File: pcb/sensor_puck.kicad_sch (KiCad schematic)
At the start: 67 parts, among them J1 DISP LEFT, J2 DISP RIGHT, J3 USB_C_Receptacle_USB2.0_16P, J5 Generic, SW1 RST, SW2 BOOT, U1 ESP32-S3-MINI-1U, U2 ST25DV16K-IER8C3, U3 LSM6DSOXTR, U4 STC31-C-R3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

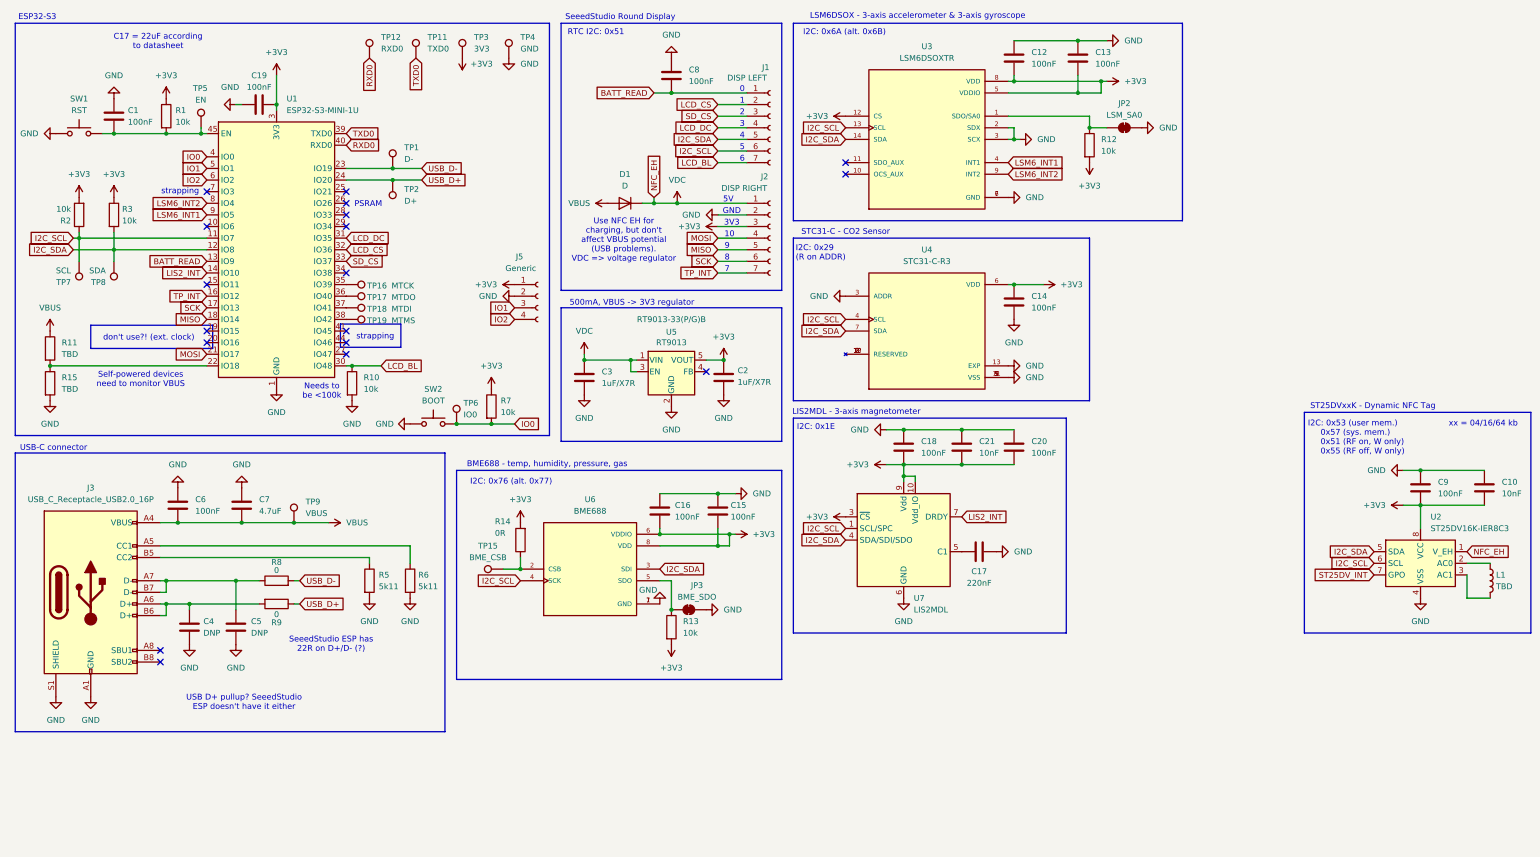
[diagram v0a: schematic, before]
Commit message: feat(schematic): add resettable fuses to VBUS and 3V3 for short protection
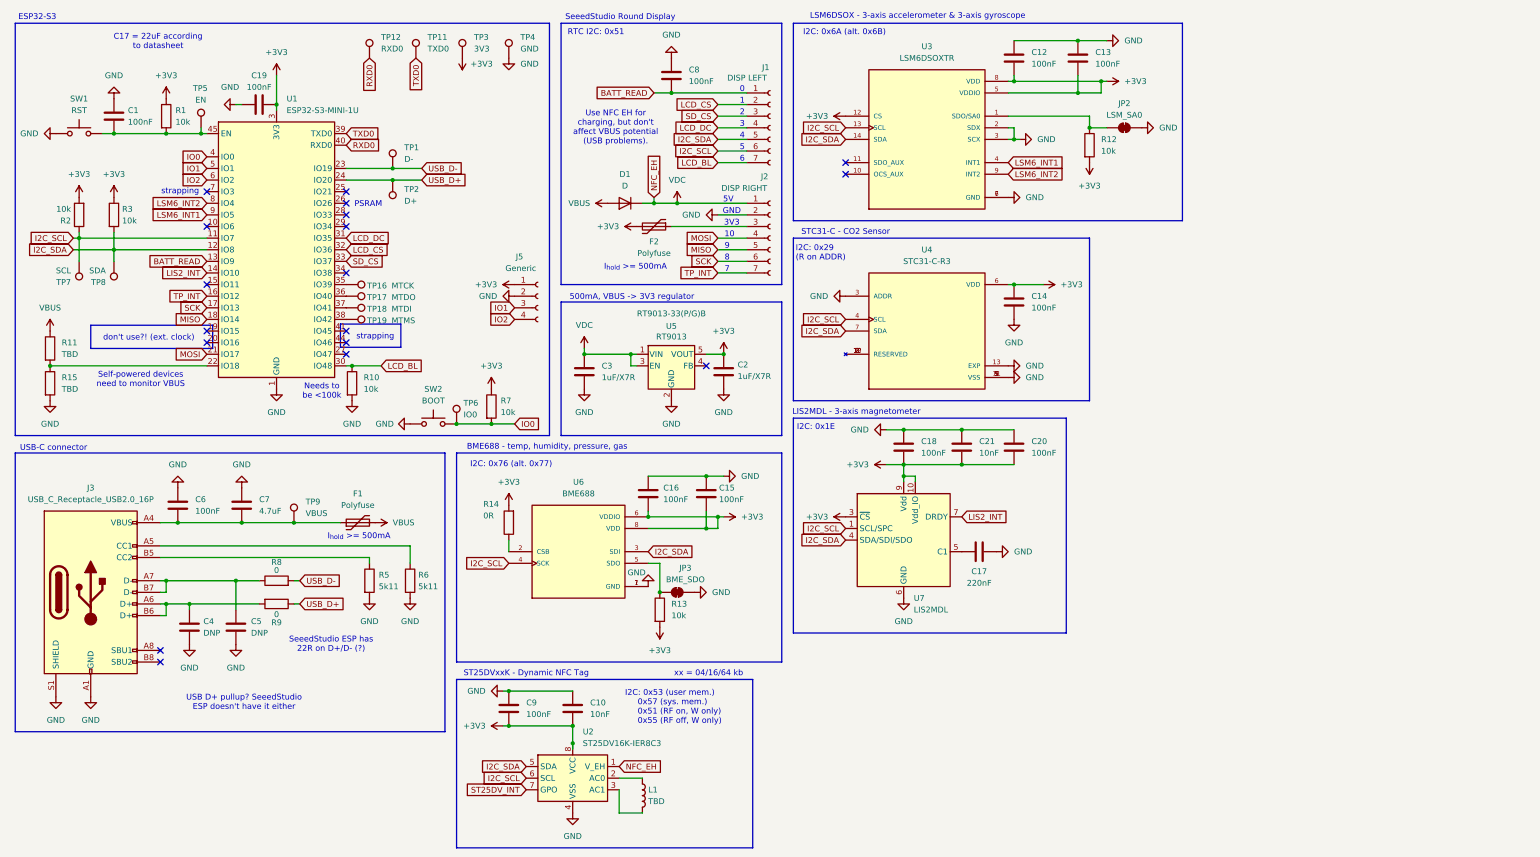
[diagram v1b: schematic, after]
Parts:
- removed TP15: BME_CSB, TestPoint:TestPoint_Pad_D1.0mm, symbol Connector:TestPoint
- added F1, F2: Polyfuse, symbol Device:Polyfuse
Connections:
- net +3V3: now also F2.2; no longer J2.3 (Pin_3)
- net VBUS: now also F1.2; no longer C6.2, C7.2, J3.A4 (VBUS), J3.A9 (VBUS), J3.B4 (VBUS), J3.B9 (VBUS), TP9.1
- new net: F2.1, J2.3 (Pin_3)
- new net: C6.2, C7.2, F1.1, J3.A4 (VBUS), J3.A9 (VBUS), J3.B4 (VBUS), J3.B9 (VBUS), TP9.1
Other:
- note added: "I_{hold} >= 500mA"
- note added: "Use NFC EH for charging, but don't affect VBUS potential (USB problems)."
- note removed: "Use NFC EH for charging, but don't affect VBUS potential (USB problems). VDC => voltage regulator"
- moved on the sheet: C10, C15, C16, C2, C3, C9, JP3, L1, R13, R14, U2, U5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

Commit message: feat(schematic): add buzzer for auditory feedback
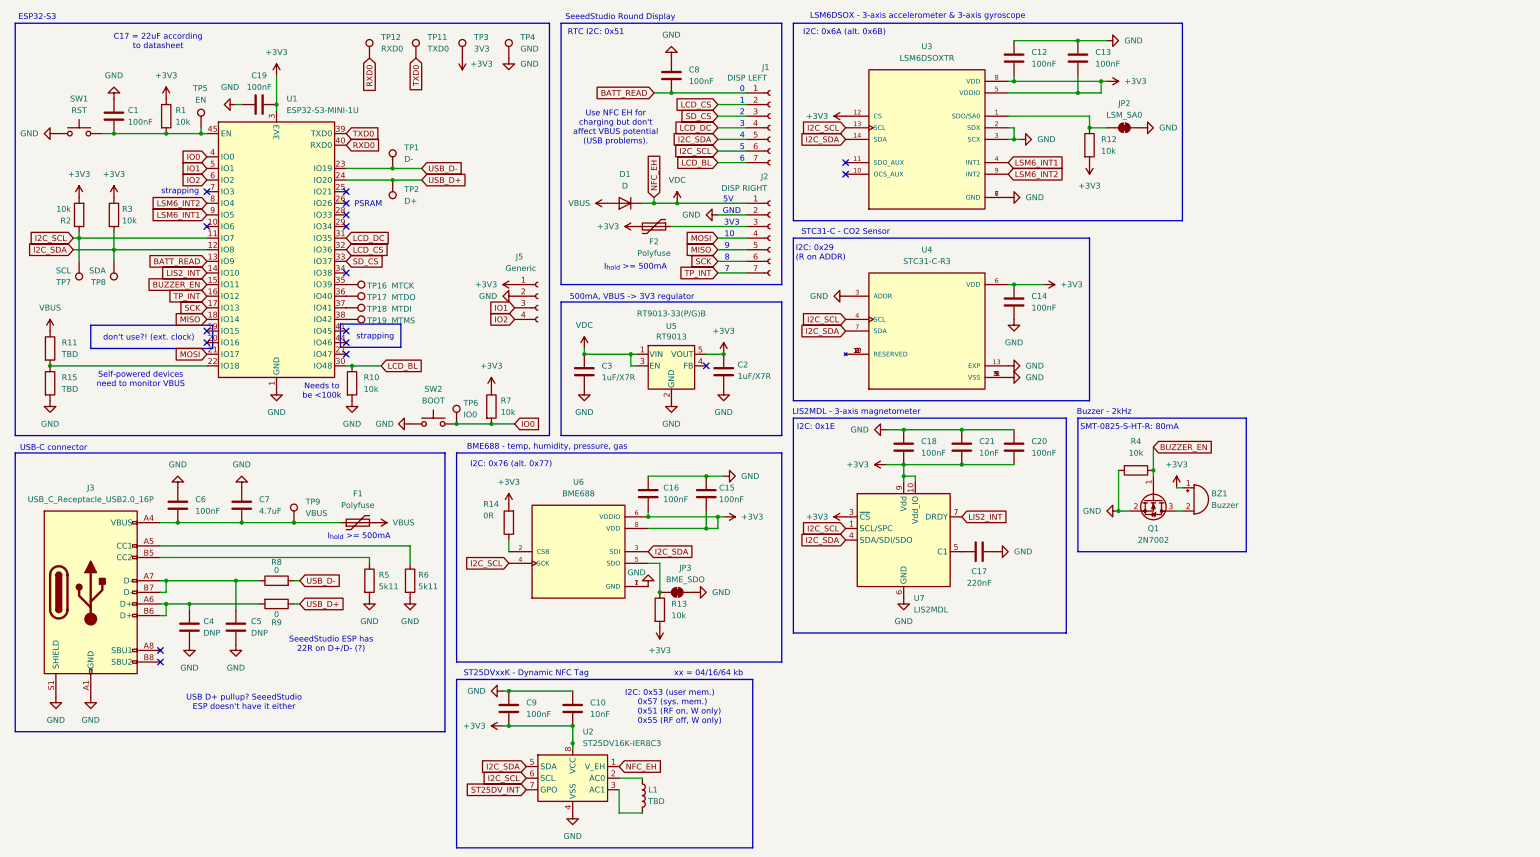
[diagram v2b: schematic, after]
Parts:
- added BZ1: Buzzer, symbol Device:Buzzer
- added Q1: 2N7002, Package_TO_SOT_SMD:SOT-23, symbol Transistor_FET:2N7002
- added R4: 10k, symbol Device:R
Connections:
- net +3V3: now also BZ1.1 (+)
- net GND: now also Q1.2 (S), R4.2
- net BUZZER_EN: now reaches U1.15 (IO11)
- net BUZZER_EN: now also Q1.1 (G), R4.1
- new net: BZ1.2 (-), Q1.3 (D)
- no-connect marks 18 -> 17
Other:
- note added: "Buzzer - 2kHz"
- note added: "SMT-0825-S-HT-R: 80mA"
- note added: "Use NFC EH for charging but don't affect VBUS potential (USB problems)."
- note removed: "Use NFC EH for charging, but don't affect VBUS potential (USB problems)."

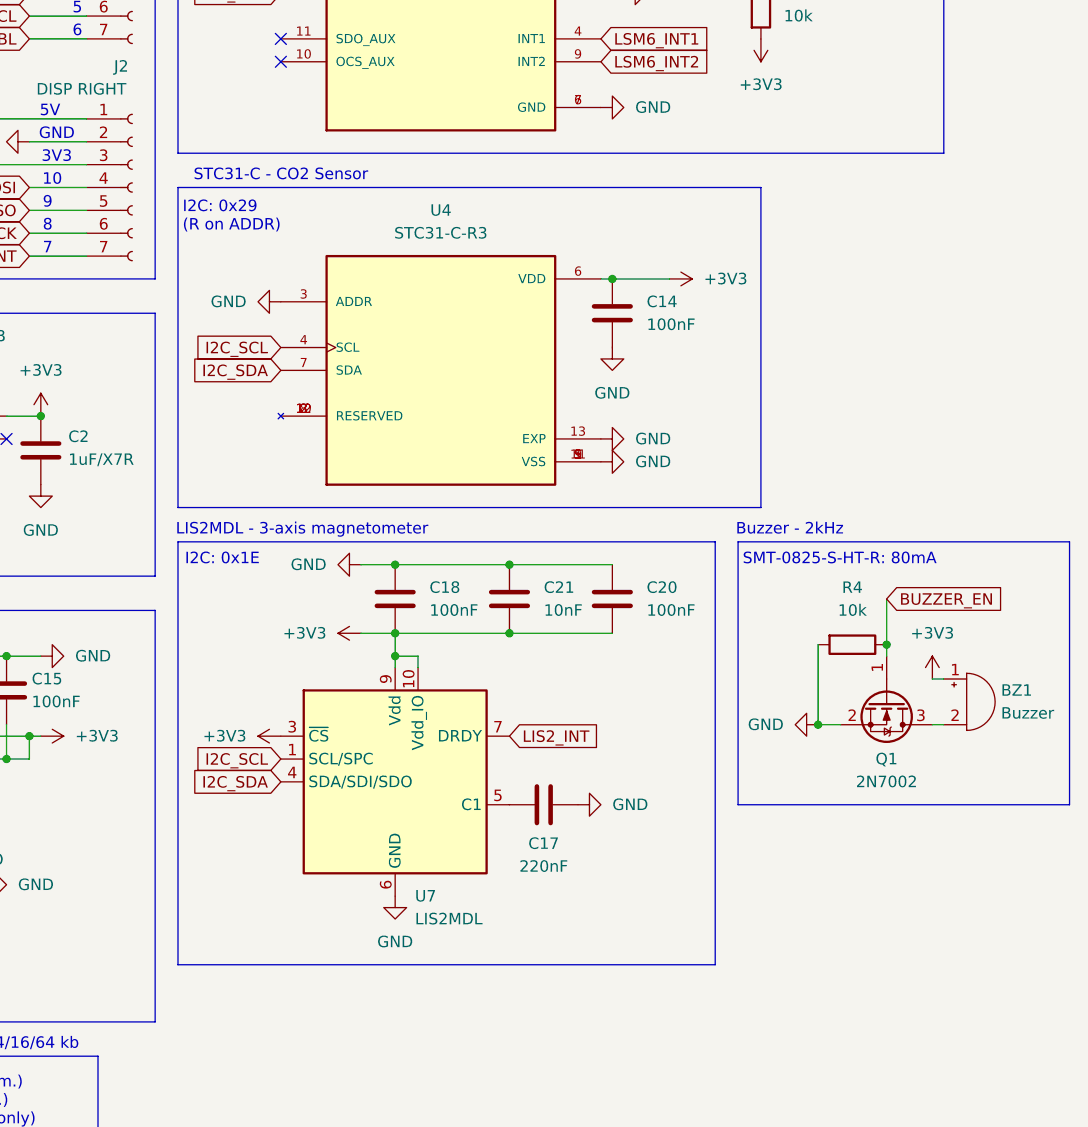
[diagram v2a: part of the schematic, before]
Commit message: feat(schematic): swap unusable STC31-C for SCD41
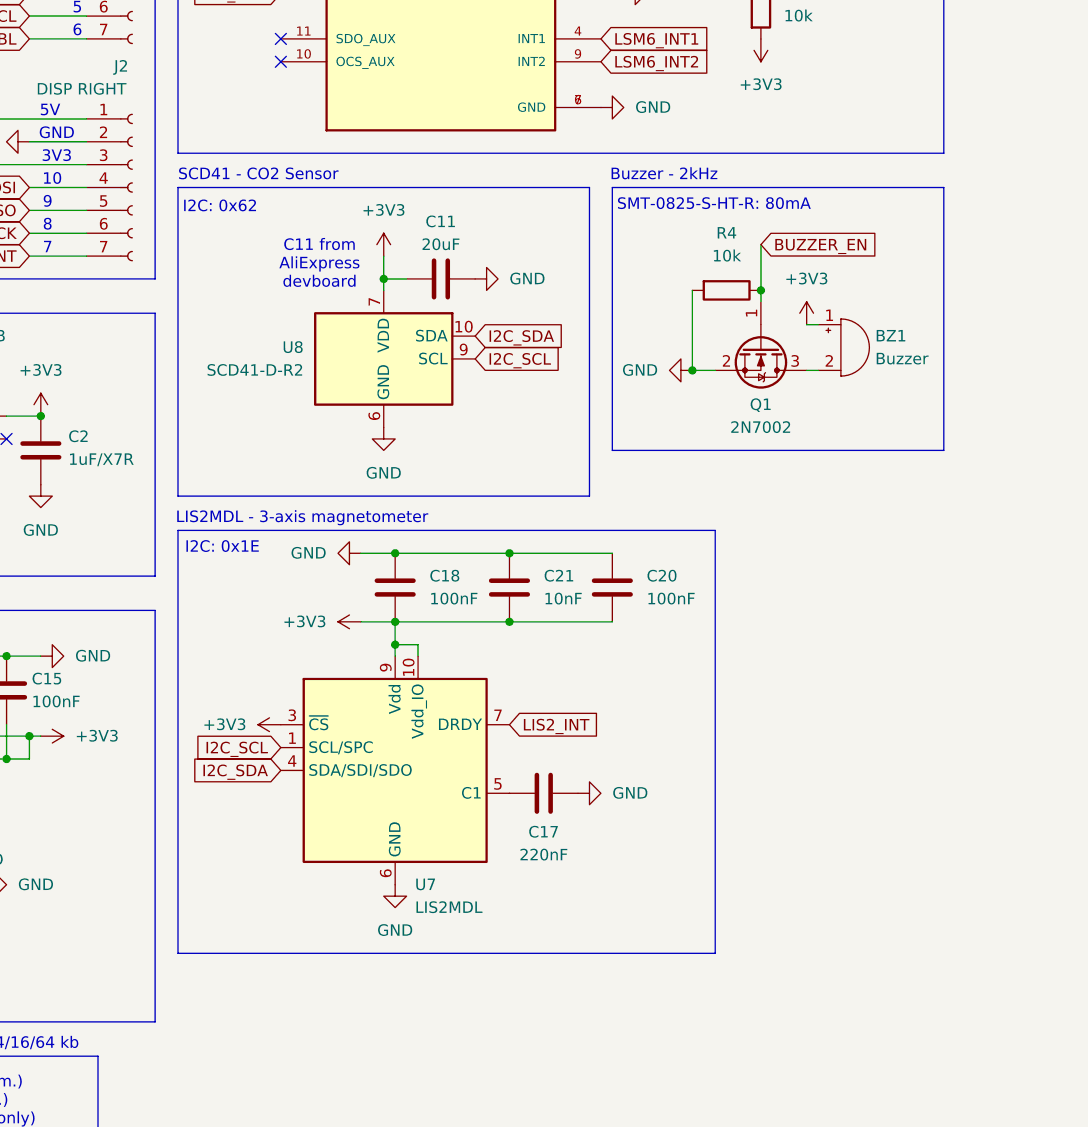
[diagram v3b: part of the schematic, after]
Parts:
- removed C14: 100nF, Capacitor_SMD:C_0805_2012Metric, symbol Device:C
- removed U4: STC31-C-R3, STC31-C:XDCR_STC31-C-R3, symbol STC31-C-R3:STC31-C-R3
- added C11: 20uF, symbol Device:C
- added U8: SCD41-D-R2, Sensor:Sensirion_SCD4x-1EP_10.1x10.1mm_P1.25mm_EP4.8x4.8mm, symbol Sensor_Gas:SCD41-D-R2
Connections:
- net +3V3: now also C11.1, U8.19 (VDD), U8.7 (VDD)
- net GND: now also C11.2, U8.20 (GND), U8.21 (GND), U8.6 (GND)
- net I2C_SCL: now also U8.9 (SCL)
- net I2C_SDA: now also U8.10 (SDA)
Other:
- note added: "C11 from AliExpress devboard"
- note added: "I2C: 0x62"
- note added: "SCD41 - CO2 Sensor"
- note removed: "I2C: 0x29 (R on ADDR)"
- note removed: "STC31-C - CO2 Sensor"
- moved on the sheet: BZ1, C17, C18, C20, C21, Q1, R4, U7

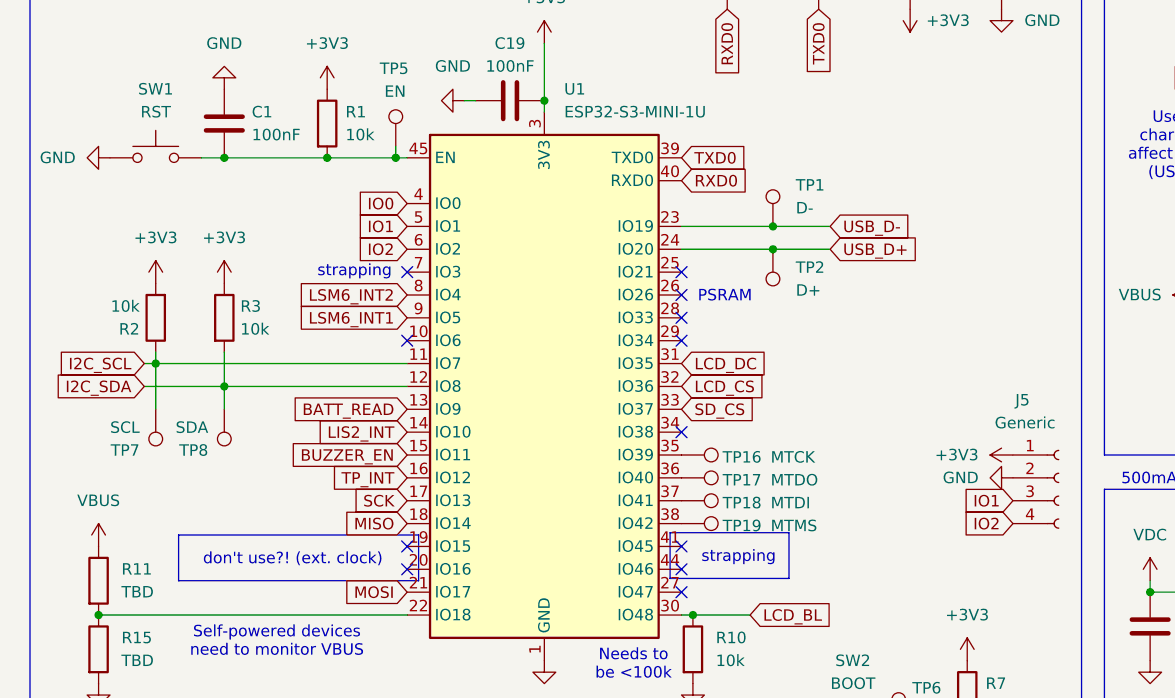
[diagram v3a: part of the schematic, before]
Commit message: fix(schematic): connect I2C lines to RTC I2C peripheral
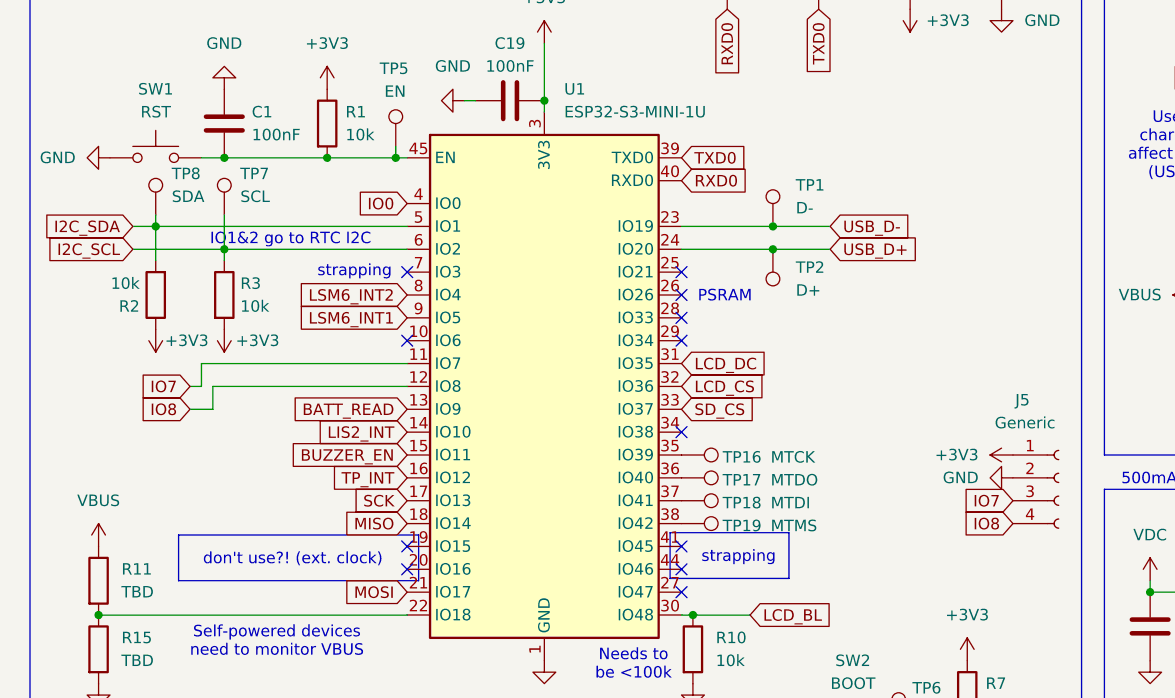
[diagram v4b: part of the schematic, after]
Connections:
- net +3V3: now also R2.1, R3.2; no longer R2.2, R3.1
- net I2C_SCL: now also R3.1, U1.6 (IO2); no longer R2.1, U1.11 (IO7)
- net I2C_SDA: now also R2.2, U1.5 (IO1); no longer R3.2, U1.12 (IO8)
- net IO1 renamed IO7
- net IO7: now also U1.11 (IO7); no longer U1.5 (IO1)
- net IO2 renamed IO8
- net IO8: now also U1.12 (IO8); no longer U1.6 (IO2)
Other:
- note added: "IO1&2 go to RTC I2C"
- moved on the sheet: R2, R3, TP7, TP8
